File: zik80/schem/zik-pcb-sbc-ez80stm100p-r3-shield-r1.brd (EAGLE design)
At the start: 160 x 100 mm, 7 parts

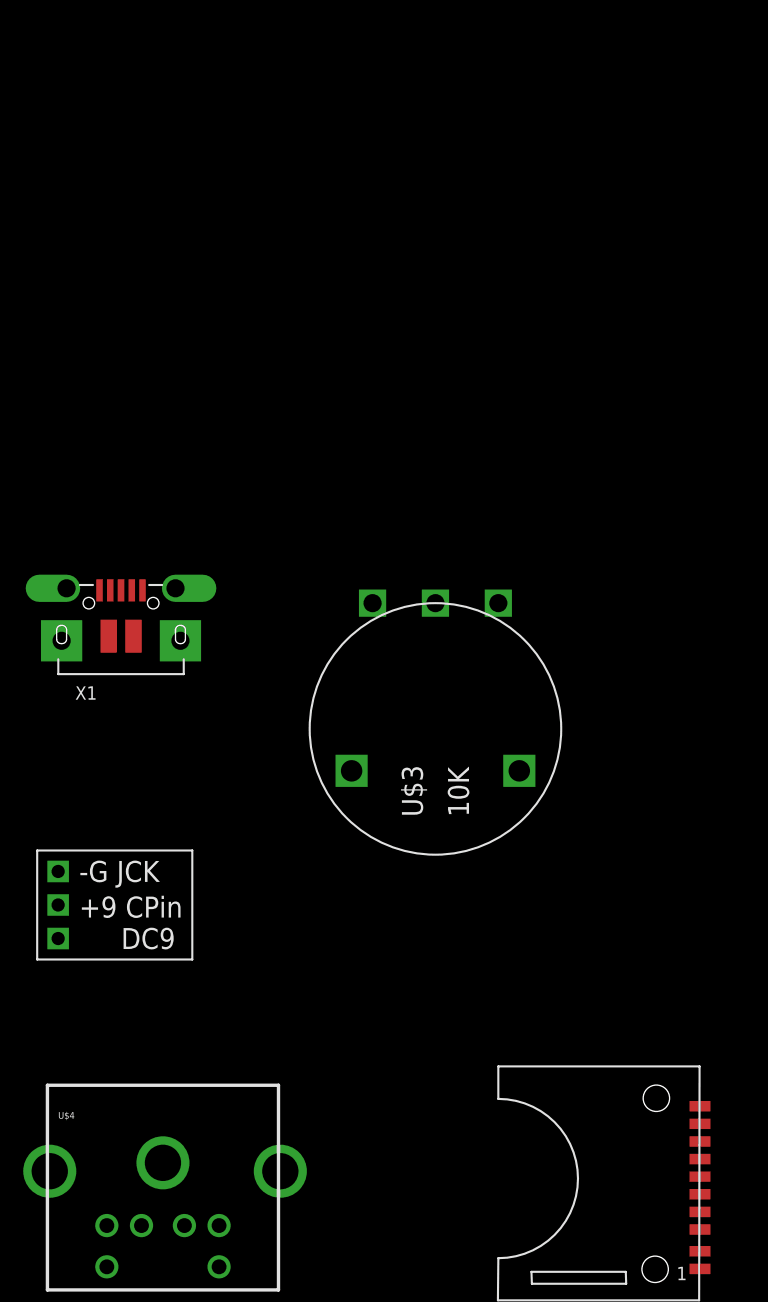
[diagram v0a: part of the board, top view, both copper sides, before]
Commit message: Updated headphone part
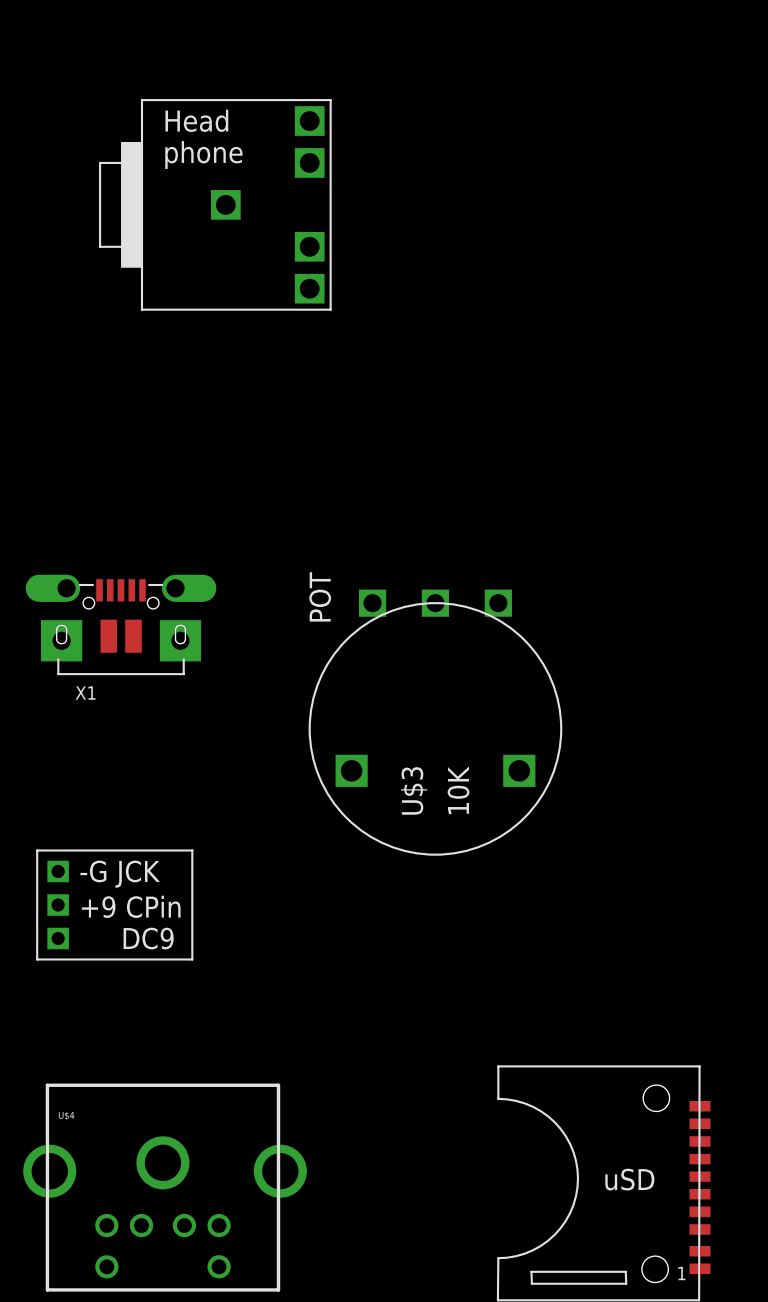
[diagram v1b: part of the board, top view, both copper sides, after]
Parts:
- added U$5: STEREOHEADPHONEJACK, skeezix:STEREOHEADPHONEJACK
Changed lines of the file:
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@@
 <setting verticaltext="up"/>
 </settings>
-<grid distance="0.05" unitdist="inch" unit="inch" style="lines" multiple="1" display="no" altdistance="0.025" altunitdist="inch" altunit="inch"/>
+<grid distance="0.05" unitdist="inch" unit="inch" style="dots" multiple="1" display="yes" altdistance="0.025" altunitdist="inch" altunit="inch"/>
 <layers>
 <layer number="1" name="Top" color="4" fill="1" visible="yes" active="yes"/>
@@
 <layer number="57" name="tCAD" color="10" fill="1" visible="no" active="no"/>
 <layer number="58" name="bCAD" color="11" fill="1" visible="no" active="no"/>
+<layer number="59" name="tCarbon" color="7" fill="1" visible="no" active="no"/>
+<layer number="60" name="bCarbon" color="7" fill="1" visible="no" active="no"/>
+<layer number="90" name="Modules" color="7" fill="1" visible="no" active="yes"/>
 <layer number="91" name="Nets" color="2" fill="1" visible="no" active="no"/>
 <layer number="92" name="Busses" color="1" fill="1" visible="no" active="no"/>
@@
 <layer number="127" name="_tValues" color="7" fill="1" visible="yes" active="yes"/>
 <layer number="128" name="_bValues" color="7" fill="1" visible="yes" active="yes"/>
+<layer number="129" name="Mask" color="7" fill="1" visible="yes" active="yes"/>
 <layer number="131" name="prix" color="7" fill="1" visible="yes" active="yes"/>
 <layer number="132" name="test" color="7" fill="1" visible="yes" active="yes"/>
@@
 <layer number="223" name="223bmp" color="24" fill="1" visible="no" active="no"/>
 <layer number="224" name="224bmp" color="25" fill="1" visible="no" active="no"/>
+<layer number="225" name="225bmp" color="7" fill="1" visible="yes" active="yes"/>
+<layer number="226" name="226bmp" color="7" fill="1" visible="yes" active="yes"/>
+<layer number="227" name="227bmp" color="7" fill="1" visible="yes" active="yes"/>
+<layer number="228" name="228bmp" color="7" fill="1" visible="yes" active="yes"/>
+<layer number="229" name="229bmp" color="7" fill="1" visible="yes" active="yes"/>
+<layer number="230" name="230bmp" color="7" fill="1" visible="yes" active="yes"/>
 <layer number="231" name="Eagle3D_PG1" color="7" fill="1" visible="yes" active="yes"/>
 <layer number="232" name="Eagle3D_PG2" color="7" fill="1" visible="yes" active="yes"/>
@@
 <layer number="251" name="SMDround" color="12" fill="11" visible="no" active="no"/>
 <layer number="254" name="cooling" color="7" fill="1" visible="yes" active="yes"/>
+<layer number="255" name="routoute" color="7" fill="1" visible="yes" active="yes"/>
 </layers>
 <board>
@@
 <element name="VGA1" library="VideoConnectors-skeemod" package="DB-15-F90+SHIELD-BIG_PADS" value="VGA-F90B" x="80.01" y="10.16"/>
 <element name="X1" library="adafruit-musb-skeemod" package="4UCONN_20329" value="" x="10.16" y="48.26"/>
+<element name="U$5" library="skeezix" package="STEREOHEADPHONEJACK" value="STEREOHEADPHONEJACK" x="10.16" y="66.04"/>
 </elements>
 <signals>
@@
 </board>
 </drawing>
+<compatibility>
+<note version="6.3" minversion="6.2.2" severity="warning">
+Since Version 6.2.2 text objects can contain more than one line,
+which will not be processed correctly with this version.
+</note>
+</compatibility>
 </eagle>

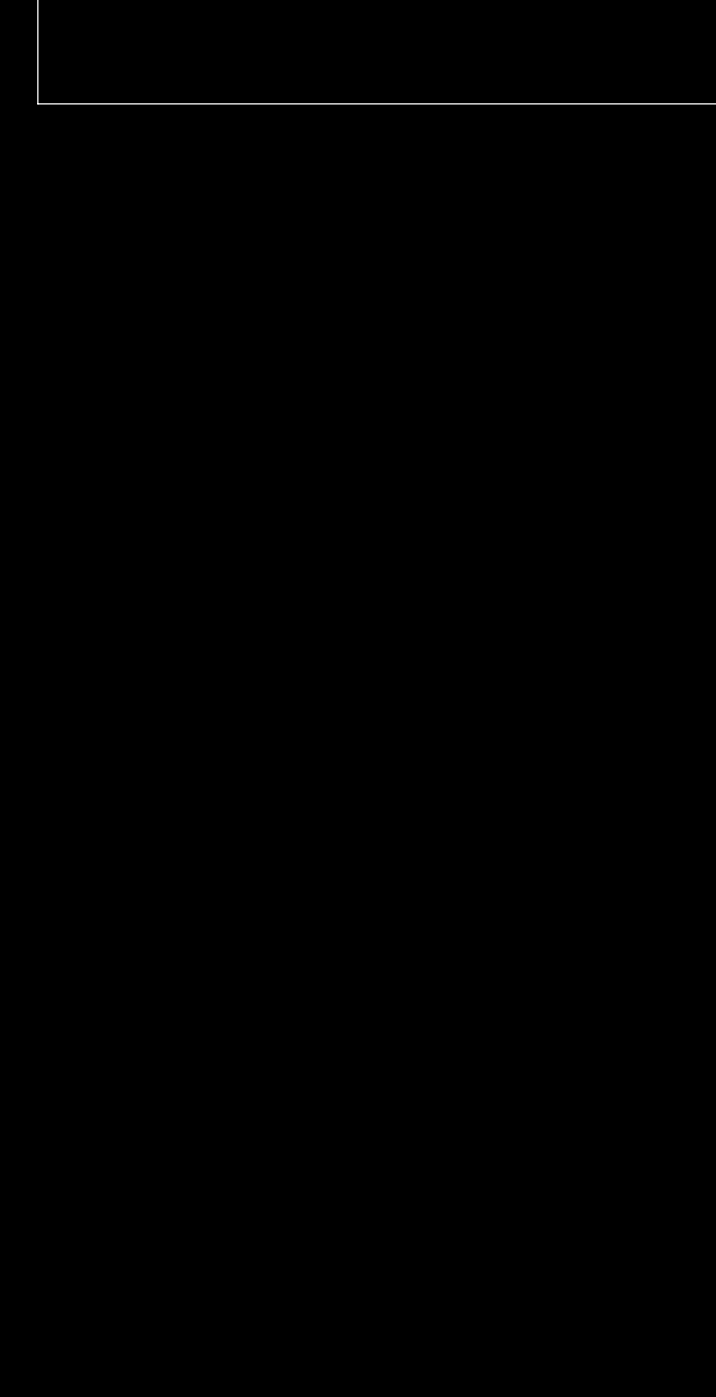
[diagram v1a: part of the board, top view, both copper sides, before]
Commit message: Dropped TPS7133QP and FTDI onto shield start
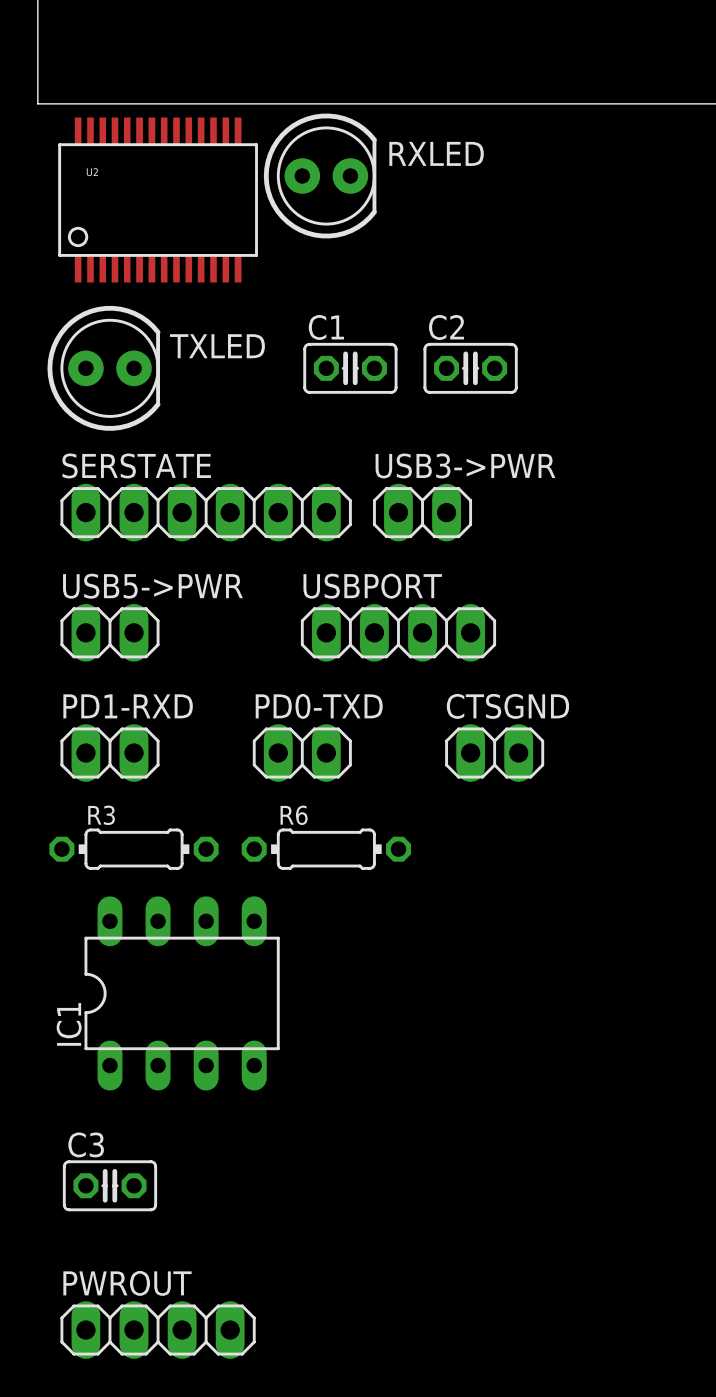
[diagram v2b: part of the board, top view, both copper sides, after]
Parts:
- added C1, C2: .1uF, rcl:C025-025X050
- added C3: 10uF Tant, rcl:C025-025X050
- added CTSGND, PD0-TXD, PD1-RXD, USB3->PWR, USB5->PWR: (no value), pinhead:1X02
- added IC1: TPS7133QP, ic-package:DIL08
- added PWROUT, USBPORT: (no value), pinhead:1X04
- added R3, R6: 330 ohm, rcl:0204/7
- added RXLED, TXLED: (no value), SparkFun-LED:LED5MM
- added SERSTATE: (no value), pinhead:1X06
- added U2: FT232RLSSOP, SparkFun:SSOP28DB
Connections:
- new net +3V3: C3.2, IC1.5, IC1.6, IC1.7, PWROUT.3
- new net CTS: CTSGND.2, SERSTATE.6, U2.11
- new net DCD: SERSTATE.2, U2.10
- new net DSR: SERSTATE.3, U2.9
- new net DTR: SERSTATE.4, U2.2
- new net FTDI3: C1.1, U2.17, USB3->PWR.1
- new net N$10: R3.2, RXLED.A
- new net N$11: R3.1, U2.22
- new net N$12: PD0-TXD.1, U2.1
- new net N$13: PD1-RXD.1, U2.5
- new net N$4: R6.2, TXLED.A
- new net N$8: R6.1, U2.23
- new net PD0: PD0-TXD.2
- new net PD1: PD1-RXD.2
- new net PWR: USB3->PWR.2, USB5->PWR.2
- new net RI: SERSTATE.1, U2.6
- new net RTS: SERSTATE.5, U2.3
- new net USB5: C2.1, U2.19, U2.20, U2.4, USB5->PWR.1, USBPORT.1
- new net USB_D+: U2.15, USBPORT.3
- new net USB_D-: U2.16, USBPORT.2
- net +5V: now also IC1.3, IC1.4, PWROUT.2
- net GND: now also C1.2, C2.2, C3.1, CTSGND.1, IC1.1, IC1.2, PWROUT.4, RXLED.K, TXLED.K, U2.18, U2.21, U2.25, U2.26, U2.7, USBPORT.4
- net VCC: now also PWROUT.1
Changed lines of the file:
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@@
 <element name="X1" library="adafruit-musb-skeemod" package="4UCONN_20329" value="" x="10.16" y="48.26"/>
 <element name="U$5" library="skeezix" package="STEREOHEADPHONEJACK" value="STEREOHEADPHONEJACK" x="10.16" y="66.04"/>
+<element name="U2" library="SparkFun" package="SSOP28DB" value="FT232RLSSOP" x="6.35" y="-5.08"/>
+<element name="USBPORT" library="pinhead" package="1X04" value="" x="19.05" y="-27.94"/>
+<element name="CTSGND" library="pinhead" package="1X02" value="" x="24.13" y="-34.29"/>
+<element name="SERSTATE" library="pinhead" package="1X06" value="" x="8.89" y="-21.59"/>
+<element name="USB5-&gt;PWR" library="pinhead" package="1X02" value="" x="3.81" y="-27.94"/>
+<element name="USB3-&gt;PWR" library="pinhead" package="1X02" value="" x="20.32" y="-21.59"/>
+<element name="TXLED" library="SparkFun-LED" package="LED5MM" value="" x="3.81" y="-13.97"/>
+<element name="RXLED" library="SparkFun-LED" package="LED5MM" value="" x="15.24" y="-3.81"/>
+<element name="C2" library="rcl" package="C025-025X050" value=".1uF" x="22.86" y="-13.97"/>
+<element name="C1" library="rcl" package="C025-025X050" value=".1uF" x="16.51" y="-13.97"/>
+<element name="R3" library="rcl" package="0204/7" value="330 ohm" x="5.08" y="-39.37"/>
+<element name="R6" library="rcl" package="0204/7" value="330 ohm" x="15.24" y="-39.37"/>
+<element name="PD0-TXD" library="pinhead" package="1X02" value="" x="13.97" y="-34.29"/>
+<element name="PD1-RXD" library="pinhead" package="1X02" value="" x="3.81" y="-34.29"/>
+<element name="IC1" library="ic-package" package="DIL08" value="TPS7133QP" x="7.62" y="-46.99"/>
+<element name="C3" library="rcl" package="C025-025X050" value="10uF Tant" x="3.81" y="-57.15"/>
+<element name="PWROUT" library="pinhead" package="1X04" value="" x="6.35" y="-64.77"/>
 </elements>
 <signals>
 <signal name="VCC">
 <contactref element="U$1" pad="CPIN"/>
-</signal>
-<signal name="GND">
+<contactref element="PWROUT" pad="1"/>
+<wire x1="6.35" y1="29.972" x2="2.54" y2="-64.77" width="0" layer="19" extent="1-1"/>
+</signal>
+<signal name="GND" class="1">
 <contactref element="U$1" pad="JACKET"/>
 <contactref element="X1" pad="SPRT@4"/>
@@
 <contactref element="X1" pad="BASE@2"/>
 <contactref element="X1" pad="SPRT@3"/>
+<contactref element="C1" pad="2"/>
+<contactref element="USBPORT" pad="4"/>
+<contactref element="U2" pad="26"/>
+<contactref element="U2" pad="25"/>
+<contactref element="U2" pad="7"/>
+<contactref element="U2" pad="18"/>
+<contactref element="U2" pad="21"/>
+<contactref element="C2" pad="2"/>
+<contactref element="CTSGND" pad="1"/>
+<contactref element="TXLED" pad="K"/>
+<contactref element="RXLED" pad="K"/>
+<contactref element="IC1" pad="1"/>
+<contactref element="IC1" pad="2"/>
+<contactref element="C3" pad="1"/>
+<contactref element="PWROUT" pad="4"/>
 <wire x1="11.46" y1="49.035" x2="13.46" y2="49.16" width="0" layer="19" extent="1-1"/>
 <wire x1="10.91" y1="46.26" x2="11.46" y2="49.035" width="0" layer="19" extent="1-1"/>
@@
 <wire x1="6.86" y1="49.16" x2="6.56" y2="45.979" width="0" layer="19" extent="1-1"/>
 <wire x1="6.35" y1="32.004" x2="6.56" y2="45.979" width="0" layer="19" extent="1-1"/>
+<wire x1="6.675" y1="-1.424" x2="6.35" y2="32.004" width="0" layer="19" extent="1-1"/>
+<wire x1="8.625" y1="-1.424" x2="6.675" y2="-1.424" width="0" layer="19" extent="1-1"/>
+<wire x1="4.075" y1="-1.424" x2="6.675" y2="-1.424" width="0" layer="19" extent="1-1"/>
+<wire x1="3.425" y1="-1.424" x2="4.075" y2="-1.424" width="0" layer="19" extent="1-1"/>
+<wire x1="6.025" y1="-8.736" x2="6.675" y2="-1.424" width="0" layer="19" extent="1-1"/>
+<wire x1="5.08" y1="-13.97" x2="6.025" y2="-8.736" width="0" layer="19" extent="1-1"/>
+<wire x1="16.51" y1="-3.81" x2="8.625" y2="-1.424" width="0" layer="19" extent="1-1"/>
+<wire x1="17.78" y1="-13.97" x2="16.51" y2="-3.81" width="0" layer="19" extent="1-1"/>
+<wire x1="24.13" y1="-13.97" x2="17.78" y2="-13.97" width="0" layer="19" extent="1-1"/>
+<wire x1="22.86" y1="-27.94" x2="24.13" y2="-13.97" width="0" layer="19" extent="1-1"/>
+<wire x1="22.86" y1="-34.29" x2="22.86" y2="-27.94" width="0" layer="19" extent="1-1"/>
+<wire x1="6.35" y1="-50.8" x2="22.86" y2="-34.29" width="0" layer="19" extent="1-1"/>
+<wire x1="3.81" y1="-50.8" x2="6.35" y2="-50.8" width="0" layer="19" extent="1-1"/>
+<wire x1="2.54" y1="-57.15" x2="3.81" y2="-50.8" width="0" layer="19" extent="1-1"/>
+<wire x1="10.16" y1="-64.77" x2="2.54" y2="-57.15" width="0" layer="19" extent="1-1"/>
 </signal>
 <signal name="+5V">
 <contactref element="VGA1" pad="9"/>
+<contactref element="IC1" pad="3"/>
+<contactref element="IC1" pad="4"/>
+<contactref element="PWROUT" pad="2"/>
+<wire x1="11.43" y1="-50.8" x2="78.613" y2="21.59" width="0" layer="19" extent="1-1"/>
+<wire x1="8.89" y1="-50.8" x2="11.43" y2="-50.8" width="0" layer="19" extent="1-1"/>
+<wire x1="5.08" y1="-64.77" x2="8.89" y2="-50.8" width="0" layer="19" extent="1-1"/>
 </signal>
 <signal name="VBUS">
 <contactref element="X1" pad="VBUS"/>
 </signal>
+<signal name="USB_D-">
+<contactref element="U2" pad="16"/>
+<contactref element="USBPORT" pad="2"/>
+<wire x1="9.925" y1="-1.424" x2="17.78" y2="-27.94" width="0" layer="19" extent="1-1"/>
+</signal>
+<signal name="USB_D+">
+<contactref element="U2" pad="15"/>
+<contactref element="USBPORT" pad="3"/>
+<wire x1="20.32" y1="-27.94" x2="10.575" y2="-1.424" width="0" layer="19" extent="1-1"/>
+</signal>
+<signal name="FTDI3" class="1">
+<contactref element="U2" pad="17"/>
+<contactref element="USB3-&gt;PWR" pad="1"/>
+<contactref element="C1" pad="1"/>
+<wire x1="15.24" y1="-13.97" x2="9.275" y2="-1.424" width="0" layer="19" extent="1-1"/>
+<wire x1="19.05" y1="-21.59" x2="15.24" y2="-13.97" width="0" layer="19" extent="1-1"/>
+</signal>
+<signal name="PWR">
+<contactref element="USB5-&gt;PWR" pad="2"/>
+<contactref element="USB3-&gt;PWR" pad="2"/>
+<wire x1="21.59" y1="-21.59" x2="5.08" y2="-27.94" width="0" layer="19" extent="1-1"/>
+</signal>
+<signal name="PD0">
+<contactref element="PD0-TXD" pad="2"/>
+</signal>
+<signal name="PD1">
+<contactref element="PD1-RXD" pad="2"/>
+</signal>
+<signal name="USB5">
+<contactref element="U2" pad="20"/>
+<contactref element="U2" pad="4"/>
+<contactref element="USBPORT" pad="1"/>
+<contactref element="U2" pad="19"/>
+<contactref element="USB5-&gt;PWR" pad="1"/>
+<contactref element="C2" pad="1"/>
+<wire x1="15.24" y1="-27.94" x2="2.54" y2="-27.94" width="0" layer="19" extent="1-1"/>
+<wire x1="21.59" y1="-13.97" x2="15.24" y2="-27.94" width="0" layer="19" extent="1-1"/>
+<wire x1="4.075" y1="-8.736" x2="21.59" y2="-13.97" width="0" layer="19" extent="1-1"/>
+<wire x1="7.325" y1="-1.424" x2="4.075" y2="-8.736" width="0" layer="19" extent="1-1"/>
+<wire x1="7.975" y1="-1.424" x2="7.325" y2="-1.424" width="0" layer="19" extent="1-1"/>
+</signal>
+<signal name="RTS">
+<contactref element="U2" pad="3"/>
+<contactref element="SERSTATE" pad="5"/>
+<wire x1="3.425" y1="-8.736" x2="12.7" y2="-21.59" width="0" layer="19" extent="1-1"/>
+</signal>
+<signal name="DTR">
+<contactref element="U2" pad="2"/>
+<contactref element="SERSTATE" pad="4"/>
+<wire x1="2.775" y1="-8.736" x2="10.16" y2="-21.59" width="0" layer="19" extent="1-1"/>
+</signal>
+<signal name="DSR">
+<contactref element="U2" pad="9"/>
+<contactref element="SERSTATE" pad="3"/>
+<wire x1="7.325" y1="-8.736" x2="7.62" y2="-21.59" width="0" layer="19" extent="1-1"/>
+</signal>
+<signal name="DCD">
+<contactref element="U2" pad="10"/>
+<contactref element="SERSTATE" pad="2"/>
+<wire x1="7.975" y1="-8.736" x2="5.08" y2="-21.59" width="0" layer="19" extent="1-1"/>
+</signal>
+<signal name="RI">
+<contactref element="U2" pad="6"/>
+<contactref element="SERSTATE" pad="1"/>
+<wire x1="5.375" y1="-8.736" x2="2.54" y2="-21.59" width="0" layer="19" extent="1-1"/>
+</signal>
+<signal name="CTS">
+<contactref element="U2" pad="11"/>
+<contactref element="CTSGND" pad="2"/>
+<contactref element="SERSTATE" pad="6"/>
+<wire x1="15.24" y1="-21.59" x2="25.4" y2="-34.29" width="0" layer="19" extent="1-1"/>
+<wire x1="8.625" y1="-8.736" x2="15.24" y2="-21.59" width="0" layer="19" extent="1-1"/>
+</signal>
+<signal name="N$4">
+<contactref element="TXLED" pad="A"/>
+<contactref element="R6" pad="2"/>
+<wire x1="2.54" y1="-13.97" x2="19.05" y2="-39.37" width="0" layer="19" extent="1-1"/>
+</signal>
+<signal name="N$8">
+<contactref element="U2" pad="23"/>
+<contactref element="R6" pad="1"/>
+<wire x1="5.375" y1="-1.424" x2="11.43" y2="-39.37" width="0" layer="19" extent="1-1"/>
+</signal>
+<signal name="N$10">
+<contactref element="RXLED" pad="A"/>
+<contactref element="R3" pad="2"/>
+<wire x1="13.97" y1="-3.81" x2="8.89" y2="-39.37" width="0" layer="19" extent="1-1"/>
+</signal>
+<signal name="N$11">
+<contactref element="U2" pad="22"/>
+<contactref element="R3" pad="1"/>
+<wire x1="6.025" y1="-1.424" x2="1.27" y2="-39.37" width="0" layer="19" extent="1-1"/>
+</signal>
+<signal name="N$12">
+<contactref element="U2" pad="1"/>
+<contactref element="PD0-TXD" pad="1"/>
+<wire x1="2.125" y1="-8.736" x2="12.7" y2="-34.29" width="0" layer="19" extent="1-1"/>
+</signal>
+<signal name="N$13">
+<contactref element="U2" pad="5"/>
+<contactref element="PD1-RXD" pad="1"/>
+<wire x1="4.725" y1="-8.736" x2="2.54" y2="-34.29" width="0" layer="19" extent="1-1"/>
+</signal>
+<signal name="+3V3">
+<contactref element="IC1" pad="5"/>
+<contactref element="C3" pad="2"/>
+<contactref element="IC1" pad="7"/>
+<contactref element="IC1" pad="6"/>
+<contactref element="PWROUT" pad="3"/>
+<wire x1="5.08" y1="-57.15" x2="7.62" y2="-64.77" width="0" layer="19" extent="1-1"/>
+<wire x1="6.35" y1="-43.18" x2="5.08" y2="-57.15" width="0" layer="19" extent="1-1"/>
+<wire x1="8.89" y1="-43.18" x2="6.35" y2="-43.18" width="0" layer="19" extent="1-1"/>
+<wire x1="11.43" y1="-43.18" x2="8.89" y2="-43.18" width="0" layer="19" extent="1-1"/>
+</signal>
 </signals>
